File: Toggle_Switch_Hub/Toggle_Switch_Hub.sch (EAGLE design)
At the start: 6 parts

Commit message: Licenses
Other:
- note added: "Toggle Switch Hub Project by Cycfi Research is licensed under a Creative Commons Attribution-ShareAlike 4.0 International License. Copyright CYCFI Research Inc. 2013-2016"
- note removed: "Toggle Switch Hub Project by Cycfi Research is licensed under a Creative Commons Attribution-NonCommercial 4.0 International License. http://creativecommons.org/licenses/by-nc/4.0/ Copyright CYCFI Research Inc. 2013-2016"
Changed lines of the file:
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@@
 <text x="253.365" y="6.985" size="2.1844" layer="95">v1.1</text>
 <text x="7.62" y="12.7" size="2.54" layer="95">Toggle Switch Hub Project by Cycfi Research is licensed under a
-Creative Commons Attribution-NonCommercial 4.0 International License.
-http://creativecommons.org/licenses/by-nc/4.0/
+Creative Commons Attribution-ShareAlike 4.0 International License.
 Copyright CYCFI Research Inc. 2013-2016</text>
 <text x="200.66" y="11.43" size="2.54" layer="95">2016038</text>
@@
 <text x="254" y="7.62" size="2.1844" layer="95">v1.1</text>
 <text x="8.255" y="13.335" size="2.54" layer="95">Toggle Switch Hub Project by Cycfi Research is licensed under a
-Creative Commons Attribution-NonCommercial 4.0 International License.
-http://creativecommons.org/licenses/by-nc/4.0/
+Creative Commons Attribution-ShareAlike 4.0 International License.
 Copyright CYCFI Research Inc. 2013-2016</text>
 <text x="201.295" y="12.065" size="2.54" layer="95">2016038</text>

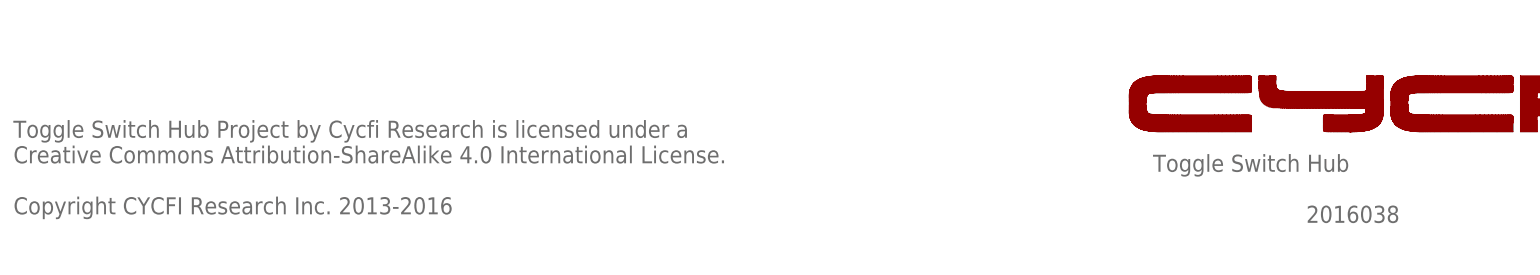
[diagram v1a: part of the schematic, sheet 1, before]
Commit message: *organize 5-waay switch and its configuration board(a and b) *update license date *remove red frame schem pdf files, change with black frame *update document number
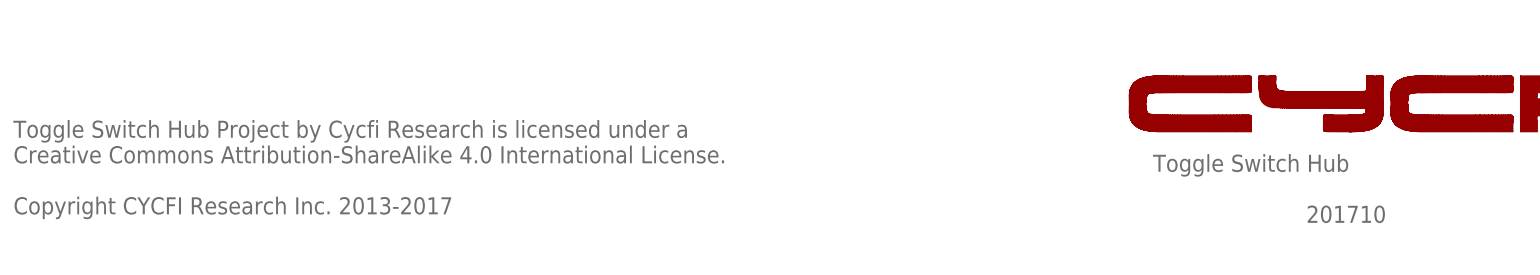
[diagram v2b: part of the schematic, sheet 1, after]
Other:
- note added: "201710"
- note added: "201711"
- note added: "Toggle Switch Hub Project by Cycfi Research is licensed under a Creative Commons Attribution-ShareAlike 4.0 International License. Copyright CYCFI Research Inc. 2013-2017"
- note removed: "2016038"
- note removed: "Toggle Switch Hub Project by Cycfi Research is licensed under a Creative Commons Attribution-ShareAlike 4.0 International License. Copyright CYCFI Research Inc. 2013-2016"
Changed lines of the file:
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@@
 <text x="7.62" y="12.7" size="2.54" layer="95">Toggle Switch Hub Project by Cycfi Research is licensed under a
 Creative Commons Attribution-ShareAlike 4.0 International License.
-Copyright CYCFI Research Inc. 2013-2016</text>
-<text x="200.66" y="11.43" size="2.54" layer="95">2016038</text>
+Copyright CYCFI Research Inc. 2013-2017</text>
+<text x="200.66" y="11.43" size="2.54" layer="95">201710</text>
 <wire x1="192.47528125" y1="25.047221875" x2="190.115640625" y2="25.047221875" width="0" layer="94"/>
 <wire x1="190.115640625" y1="25.047221875" x2="188.10833125" y2="25.047225" width="0" layer="94"/>
@@
 <text x="8.255" y="13.335" size="2.54" layer="95">Toggle Switch Hub Project by Cycfi Research is licensed under a
 Creative Commons Attribution-ShareAlike 4.0 International License.
-Copyright CYCFI Research Inc. 2013-2016</text>
-<text x="201.295" y="12.065" size="2.54" layer="95">2016038</text>
+Copyright CYCFI Research Inc. 2013-2017</text>
+<text x="201.295" y="12.065" size="2.54" layer="95">201711</text>
 <wire x1="193.11028125" y1="25.682221875" x2="190.750640625" y2="25.682221875" width="0" layer="94"/>
 <wire x1="190.750640625" y1="25.682221875" x2="188.74333125" y2="25.682225" width="0" layer="94"/>
